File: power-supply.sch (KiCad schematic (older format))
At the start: 108 parts, among them IC1 TPS54561, J12 S2B-PH-K-S_LF__SN_, Q1 BSS138APW, Q2 BSS138APW, Q3 BSS138APW, Q4 BSS138APW, Q5 BSS138APW, U10 TPS62823DLCT, U11 TPS62823DLCT, U12 TPS62823DLCT, U13 TPS62823DLCT, U16 TPS62823DLCT, U9 LM3881MME_NOPB

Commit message: Generated local libs
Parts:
- L2, L3, L4, L5, L6: footprint antmicro-footprints:IHLP-1212AE -> artix-dc-scm-footprints:IHLP-1212AE; symbol antmicroFixedInductors:IHLP1212AEERR47M11 -> artix-dc-scm:IHLP1212AEERR47M11
- Q1, Q2, Q3, Q4, Q5: footprint antmicro-footprints:SC70-3 -> artix-dc-scm-footprints:SC70-3; symbol antmicroTransistorsFETsMOSFETsSingle:BSS138APW -> artix-dc-scm:BSS138APW
- Q6: renamed from Q?; footprint antmicro-footprints:SC70-3 -> artix-dc-scm-footprints:SC70-3; symbol antmicroTransistorsFETsMOSFETsSingle:BSS138APW -> artix-dc-scm:BSS138APW
- R139, R140, R141, R142, R188: footprint antmicro-footprints:0603-res -> artix-dc-scm-footprints:0603-res; symbol antmicroResistors0603:R_0R_0603 -> artix-dc-scm:R_0R_0603
- gave numbers to parts that had none: 3
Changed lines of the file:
@@
 $EndComp
 $Comp
-L antmicroFixedInductors:IHLP1212AEERR47M11 L2
+L artix-dc-scm:IHLP1212AEERR47M11 L2
 U 1 1 605967EC
 P 14275 1350
 F 0 "L2" H 14275 1564 60  0000 C CNN
 F 1 "IHLP1212AEERR47M11" H 14275 1458 60  0000 C CNN
-F 2 "antmicro-footprints:IHLP-1212AE" H 14275 1350 60  0001 C CNN
+F 2 "artix-dc-scm-footprints:IHLP-1212AE" H 14275 1350 60  0001 C CNN
 F 3 "" H 14275 1350 60  0001 C CNN
 F 4 "Vishay" H 14275 1350 50  0001 C CNN "Manufacturer"
@@
 $EndComp
 $Comp
-L antmicroFixedInductors:IHLP1212AEERR47M11 L3
+L artix-dc-scm:IHLP1212AEERR47M11 L3
 U 1 1 605975DC
 P 14300 3275
 F 0 "L3" H 14175 3500 60  0000 C CNN
 F 1 "IHLP1212AEERR47M11" H 14625 3375 60  0000 C CNN
-F 2 "antmicro-footprints:IHLP-1212AE" H 14300 3275 60  0001 C CNN
+F 2 "artix-dc-scm-footprints:IHLP-1212AE" H 14300 3275 60  0001 C CNN
 F 3 "" H 14300 3275 60  0001 C CNN
 F 4 "Vishay" H 14300 3275 50  0001 C CNN "Manufacturer"
@@
 $EndComp
 $Comp
-L antmicroFixedInductors:IHLP1212AEERR47M11 L5
+L artix-dc-scm:IHLP1212AEERR47M11 L5
 U 1 1 605987A7
 P 14350 5100
 F 0 "L5" H 14200 5300 60  0000 C CNN
 F 1 "IHLP1212AEERR47M11" H 14650 5200 60  0000 C CNN
-F 2 "antmicro-footprints:IHLP-1212AE" H 14350 5100 60  0001 C CNN
+F 2 "artix-dc-scm-footprints:IHLP-1212AE" H 14350 5100 60  0001 C CNN
 F 3 "" H 14350 5100 60  0001 C CNN
 F 4 "Vishay" H 14350 5100 50  0001 C CNN "Manufacturer"
@@
 $EndComp
 $Comp
-L antmicroFixedInductors:IHLP1212AEERR47M11 L4
+L artix-dc-scm:IHLP1212AEERR47M11 L4
 U 1 1 605995D0
 P 14325 6825
 F 0 "L4" H 14200 7025 60  0000 C CNN
 F 1 "IHLP1212AEERR47M11" H 14650 6925 60  0000 C CNN
-F 2 "antmicro-footprints:IHLP-1212AE" H 14325 6825 60  0001 C CNN
+F 2 "artix-dc-scm-footprints:IHLP-1212AE" H 14325 6825 60  0001 C CNN
 F 3 "" H 14325 6825 60  0001 C CNN
 F 4 "Vishay" H 14325 6825 50  0001 C CNN "Manufacturer"
@@
 $EndComp
 $Comp
-L antmicroResistors0603:R_0R_0603 R139
+L artix-dc-scm:R_0R_0603 R139
 U 1 1 605E7324
 P 15225 1100
 F 0 "R139" V 15180 1170 60  0000 L CNN
 F 1 "R_0R_0603" H 15225 950 60  0001 C CNN
-F 2 "antmicro-footprints:0603-res" H 15425 1300 60  0001 L CNN
+F 2 "artix-dc-scm-footprints:0603-res" H 15425 1300 60  0001 L CNN
 F 3 "" H 15225 1100 50  0001 C CNN
 F 4 "BOURNS" H 15425 1500 60  0001 L CNN "Manufacturer"
@@
 $EndComp
 $Comp
-L antmicroResistors0603:R_0R_0603 R140
+L artix-dc-scm:R_0R_0603 R140
 U 1 1 605E78C4
 P 15250 3025
 F 0 "R140" V 15205 3095 60  0000 L CNN
 F 1 "R_0R_0603" H 15250 2875 60  0001 C CNN
-F 2 "antmicro-footprints:0603-res" H 15450 3225 60  0001 L CNN
+F 2 "artix-dc-scm-footprints:0603-res" H 15450 3225 60  0001 L CNN
 F 3 "" H 15250 3025 50  0001 C CNN
 F 4 "BOURNS" H 15450 3425 60  0001 L CNN "Manufacturer"
@@
 $EndComp
 $Comp
-L antmicroResistors0603:R_0R_0603 R142
+L artix-dc-scm:R_0R_0603 R142
 U 1 1 605E80F5
 P 15300 4800
 F 0 "R142" V 15255 4870 60  0000 L CNN
 F 1 "R_0R_0603" H 15300 4650 60  0001 C CNN
-F 2 "antmicro-footprints:0603-res" H 15500 5000 60  0001 L CNN
+F 2 "artix-dc-scm-footprints:0603-res" H 15500 5000 60  0001 L CNN
 F 3 "" H 15300 4800 50  0001 C CNN
 F 4 "BOURNS" H 15500 5200 60  0001 L CNN "Manufacturer"
@@
 $EndComp
 $Comp
-L antmicroResistors0603:R_0R_0603 R141
+L artix-dc-scm:R_0R_0603 R141
 U 1 1 605E88AA
 P 15275 6575
 F 0 "R141" V 15230 6645 60  0000 L CNN
 F 1 "R_0R_0603" H 15275 6425 60  0001 C CNN
-F 2 "antmicro-footprints:0603-res" H 15475 6775 60  0001 L CNN
+F 2 "artix-dc-scm-footprints:0603-res" H 15475 6775 60  0001 L CNN
 F 3 "" H 15275 6575 50  0001 C CNN
 F 4 "BOURNS" H 15475 6975 60  0001 L CNN "Manufacturer"
@@
 $EndComp
 $Comp
-L antmicroTransistorsFETsMOSFETsSingle:BSS138APW Q3
+L artix-dc-scm:BSS138APW Q3
 U 1 1 6063EBAE
 P 10275 3975
 F 0 "Q3" H 10383 4028 60  0000 L CNN
 F 1 "BSS138APW" H 10383 3922 60  0000 L CNN
-F 2 "antmicro-footprints:SC70-3" H 10475 4175 60  0001 L CNN
+F 2 "artix-dc-scm-footprints:SC70-3" H 10475 4175 60  0001 L CNN
 F 3 "" H 10475 4275 60  0001 L CNN
 F 4 "BSS138PW" H 10475 4475 60  0001 L CNN "MPN"
@@
 $EndComp
 $Comp
-L antmicroTransistorsFETsMOSFETsSingle:BSS138APW Q4
+L artix-dc-scm:BSS138APW Q4
 U 1 1 60643F19
 P 10300 5200
 F 0 "Q4" H 10408 5253 60  0000 L CNN
 F 1 "BSS138APW" H 10408 5147 60  0000 L CNN
-F 2 "antmicro-footprints:SC70-3" H 10500 5400 60  0001 L CNN
+F 2 "artix-dc-scm-footprints:SC70-3" H 10500 5400 60  0001 L CNN
 F 3 "" H 10500 5500 60  0001 L CNN
 F 4 "BSS138PW" H 10500 5700 60  0001 L CNN "MPN"
@@
 $EndComp
 $Comp
-L antmicroTransistorsFETsMOSFETsSingle:BSS138APW Q1
+L artix-dc-scm:BSS138APW Q1
 U 1 1 60644AF4
 P 10250 6475
 F 0 "Q1" H 10358 6528 60  0000 L CNN
 F 1 "BSS138APW" H 10358 6422 60  0000 L CNN
-F 2 "antmicro-footprints:SC70-3" H 10450 6675 60  0001 L CNN
+F 2 "artix-dc-scm-footprints:SC70-3" H 10450 6675 60  0001 L CNN
 F 3 "" H 10450 6775 60  0001 L CNN
 F 4 "BSS138PW" H 10450 6975 60  0001 L CNN "MPN"
@@
 $EndComp
 $Comp
-L antmicroTransistorsFETsMOSFETsSingle:BSS138APW Q2
+L artix-dc-scm:BSS138APW Q2
 U 1 1 606455AB
 P 10250 7675
 F 0 "Q2" H 10358 7728 60  0000 L CNN
 F 1 "BSS138APW" H 10358 7622 60  0000 L CNN
-F 2 "antmicro-footprints:SC70-3" H 10450 7875 60  0001 L CNN
+F 2 "artix-dc-scm-footprints:SC70-3" H 10450 7875 60  0001 L CNN
 F 3 "" H 10450 7975 60  0001 L CNN
 F 4 "BSS138PW" H 10450 8175 60  0001 L CNN "MPN"
@@
 $EndComp
 $Comp
-L antmicroTransistorsFETsMOSFETsSingle:BSS138APW Q5
+L artix-dc-scm:BSS138APW Q5
 U 1 1 60646CF6
 P 10325 2750
 F 0 "Q5" H 10433 2803 60  0000 L CNN
 F 1 "BSS138APW" H 10433 2697 60  0000 L CNN
-F 2 "antmicro-footprints:SC70-3" H 10525 2950 60  0001 L CNN
+F 2 "artix-dc-scm-footprints:SC70-3" H 10525 2950 60  0001 L CNN
 F 3 "" H 10525 3050 60  0001 L CNN
 F 4 "BSS138PW" H 10525 3250 60  0001 L CNN "MPN"
@@
 	12275 8700 11875 8700
 $Comp
-L antmicroFixedInductors:IHLP1212AEERR47M11 L6
+L artix-dc-scm:IHLP1212AEERR47M11 L6
 U 1 1 6013632B
 P 14325 8550
 F 0 "L6" H 14200 8750 60  0000 C CNN
 F 1 "IHLP1212AEERR47M11" H 14650 8650 60  0000 C CNN
-F 2 "antmicro-footprints:IHLP-1212AE" H 14325 8550 60  0001 C CNN
+F 2 "artix-dc-scm-footprints:IHLP-1212AE" H 14325 8550 60  0001 C CNN
 F 3 "" H 14325 8550 60  0001 C CNN
 F 4 "Vishay" H 14325 8550 50  0001 C CNN "Manufacturer"
@@
 $EndComp
 $Comp
-L antmicroResistors0603:R_0R_0603 R188
+L artix-dc-scm:R_0R_0603 R188
 U 1 1 60136334
 P 15275 8300
 F 0 "R188" V 15230 8370 60  0000 L CNN
 F 1 "R_0R_0603" H 15275 8150 60  0001 C CNN
-F 2 "antmicro-footprints:0603-res" H 15475 8500 60  0001 L CNN
+F 2 "artix-dc-scm-footprints:0603-res" H 15475 8500 60  0001 L CNN
 F 3 "" H 15275 8300 50  0001 C CNN
 F 4 "BOURNS" H 15475 8700 60  0001 L CNN "Manufacturer"
@@
 	10325 1150 10325 1450
 $Comp
-L artix-dc-scm:R_10k_0402 R?
+L artix-dc-scm:R_10k_0402 R189
 U 1 1 60252526
 P 9725 1425
-F 0 "R?" V 9575 1450 60  0000 L CNN
+F 0 "R189" V 9575 1450 60  0000 L CNN
 F 1 "R_10k_0402" H 9725 1275 60  0001 C CNN
 F 2 "artix-dc-scm-footprints:0402-res" H 9925 1625 60  0001 L CNN
@@
 	9725 1575 9725 1750
 $Comp
-L artix-dc-scm:LG_L29K-G2J1-24-Z D?
+L artix-dc-scm:LG_L29K-G2J1-24-Z D14
 U 1 1 60252530
 P 10525 1150
-F 0 "D?" H 10550 1050 60  0000 L CNN
+F 0 "D14" H 10550 1050 60  0000 L CNN
 F 1 "LG_L29K-G2J1-24-Z" H 9650 1375 60  0000 L CNN
 F 2 "artix-dc-scm-footprints:LED_0603" H 10725 1350 60  0001 L CNN
@@
 	10725 1150 10825 1150
 $Comp
-L artix-dc-scm:R_1k_0402 R?
+L artix-dc-scm:R_1k_0402 R190
 U 1 1 6025253B
 P 10975 1150
-F 0 "R?" H 10925 1250 60  0000 C CNN
+F 0 "R190" H 10925 1250 60  0000 C CNN
 F 1 "R_1k_0402" H 10975 1000 60  0001 C CNN
 F 2 "artix-dc-scm-footprints:0402-res" H 11175 1350 60  0001 L CNN
@@
 	11125 1150 11225 1150
 $Comp
-L artix-dc-scm:GND-artix-dc-scm #PWR?
+L artix-dc-scm:GND-artix-dc-scm #PWR06
 U 1 1 60252543
 P 10325 1950
-F 0 "#PWR?" H 10325 1700 50  0001 C CNN
+F 0 "#PWR06" H 10325 1700 50  0001 C CNN
 F 1 "GND" H 10330 1777 50  0000 C CNN
 F 2 "" H 10325 1950 50  0001 C CNN
@@
 VCC5V0
 $Comp
-L antmicroTransistorsFETsMOSFETsSingle:BSS138APW Q?
+L artix-dc-scm:BSS138APW Q6
 U 1 1 60252551
 P 10325 1650
-F 0 "Q?" H 10433 1703 60  0000 L CNN
+F 0 "Q6" H 10433 1703 60  0000 L CNN
 F 1 "BSS138APW" H 10433 1597 60  0000 L CNN
-F 2 "antmicro-footprints:SC70-3" H 10525 1850 60  0001 L CNN
+F 2 "artix-dc-scm-footprints:SC70-3" H 10525 1850 60  0001 L CNN
 F 3 "" H 10525 1950 60  0001 L CNN
 F 4 "BSS138PW" H 10525 2150 60  0001 L CNN "MPN"

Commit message: Cleaned up schematics
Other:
- note removed: "TODO: decide when should this voltage be enabled\n(power sequencer)"
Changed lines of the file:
@@
 Wire Wire Line
 	14575 1350 14875 1350
-Text Notes 14850 1025 0    50   ~ 0
+Text Notes 14850 1075 0    50   ~ 0
 3.3V/3A
 NoConn ~ -625 5725
@@
 U 1 1 60F104BF
 P 5725 4350
-F 0 "D3" H 5808 4403 60  0000 L CNN
-F 1 "PDS760-13" H 5650 4250 60  0000 L CNN
+F 0 "D3" H 5600 4250 60  0000 L CNN
+F 1 "PDS760-13" V 5850 4050 60  0000 L CNN
 F 2 "artix-dc-scm-footprints:PDS760-13" H 5725 4350 60  0001 C CNN
 F 3 "" H 5725 4350 60  0001 C CNN
@@
 Wire Wire Line
 	7150 4425 7150 4600
-Text Notes 3750 2750 0    118  ~ 0
+Text Notes 3750 2750 0    118  ~ 24
 MainSupply (5V 5A)
 $Comp
@@
 Wire Wire Line
 	12975 5400 13300 5400
-Text Notes 15475 3075 0    50   ~ 0
+Text Notes 14875 3000 0    50   ~ 0
 1.8V/3A
-Text Notes 15625 4850 0    50   ~ 0
+Text Notes 14875 4775 0    50   ~ 0
 1.35V/3A
 Connection ~ 14200 5900
@@
 	1    0    0    -1
 $EndComp
-Text Notes 9450 825  0    118  ~ 0
+Text Notes 9450 825  0    118  ~ 24
 PWR_LED Indicators
 Wire Notes Line
@@
 Text Label 5600 9100 2    50   ~ 0
 VCCIO_EN
-Text Notes 13125 950  0    118  ~ 0
+Text Notes 13125 950  0    118  ~ 24
 3V3 supply
-Text Notes 13200 2825 0    118  ~ 0
+Text Notes 13200 2825 0    118  ~ 24
 1V8 supply
-Text Notes 13150 4750 0    118  ~ 0
+Text Notes 13150 4750 0    118  ~ 24
 1V35 supply
 Wire Wire Line
@@
 Wire Wire Line
 	12950 7125 13275 7125
-Text Notes 15675 6575 0    50   ~ 0
+Text Notes 14900 6550 0    50   ~ 0
 1.0V/3A
 Connection ~ 14175 7625
@@
 	1    0    0    -1
 $EndComp
-Text Notes 13125 6475 0    118  ~ 0
+Text Notes 13125 6475 0    118  ~ 24
 1V0 supply
 Wire Wire Line
@@
 U 1 1 6113B8AB
 P 4500 9000
-F 0 "U9" H 4250 9325 50  0000 C CNN
-F 1 "LM3881MME_NOPB" H 4575 9275 50  0000 C CNN
+F 0 "U9" H 4475 9350 50  0000 C CNN
+F 1 "LM3881MME_NOPB" H 4475 9250 50  0000 C CNN
 F 2 "artix-dc-scm-footprints:VSSOP8-Texas_Instruments-DGK0008A" H 4500 9400 50  0001 L CNN
 F 3 "http://www.ti.com/lit/ds/symlink/lm3881.pdf" H 4500 9500 50  0001 L CNN
@@
 U 1 1 5FFECF1E
 P 4975 8575
-F 0 "R63" V 4930 8645 60  0000 L CNN
+F 0 "R63" H 5100 8550 60  0000 L CNN
 F 1 "R_1k_0402" H 4975 8425 60  0001 C CNN
 F 2 "artix-dc-scm-footprints:0402-res" H 5175 8775 60  0001 L CNN
@@
 F 4 "BOURNS" H 5175 8975 60  0001 L CNN "Manufacturer"
 F 5 "CR0402-FX-1001GLF" H 5175 8875 60  0001 L CNN "MPN"
-F 6 "1k" V 5028 8645 50  0000 L CNN "Val"
+F 6 "1k" H 4950 8575 50  0000 L CNN "Val"
 	1    4975 8575
 	0    1    1    0
@@
 U 1 1 5FFED382
 P 5075 8575
-F 0 "R64" V 5030 8645 60  0000 L CNN
+F 0 "R64" H 5200 8550 60  0000 L CNN
 F 1 "R_1k_0402" H 5075 8425 60  0001 C CNN
 F 2 "artix-dc-scm-footprints:0402-res" H 5275 8775 60  0001 L CNN
@@
 F 4 "BOURNS" H 5275 8975 60  0001 L CNN "Manufacturer"
 F 5 "CR0402-FX-1001GLF" H 5275 8875 60  0001 L CNN "MPN"
-F 6 "1k" V 5128 8645 50  0000 L CNN "Val"
+F 6 "1k" H 5050 8575 50  0000 L CNN "Val"
 	1    5075 8575
 	0    1    1    0
@@
 U 1 1 5FFED63B
 P 5175 8575
-F 0 "R65" V 5130 8645 60  0000 L CNN
+F 0 "R65" H 5300 8550 60  0000 L CNN
 F 1 "R_1k_0402" H 5175 8425 60  0001 C CNN
 F 2 "artix-dc-scm-footprints:0402-res" H 5375 8775 60  0001 L CNN
@@
 F 4 "BOURNS" H 5375 8975 60  0001 L CNN "Manufacturer"
 F 5 "CR0402-FX-1001GLF" H 5375 8875 60  0001 L CNN "MPN"
-F 6 "1k" V 5228 8645 50  0000 L CNN "Val"
+F 6 "1k" H 5150 8575 50  0000 L CNN "Val"
 	1    5175 8575
 	0    1    1    0
@@
 U 1 1 60986D60
 P 10525 2250
-F 0 "D8" H 10550 2150 60  0000 L CNN
+F 0 "D8" H 10450 2100 60  0000 L CNN
 F 1 "LG_L29K-G2J1-24-Z" H 9650 2475 60  0000 L CNN
 F 2 "artix-dc-scm-footprints:LED_0603" H 10725 2450 60  0001 L CNN
@@
 U 1 1 60986D95
 P 10475 3475
-F 0 "D6" H 10500 3375 60  0000 L CNN
+F 0 "D6" H 10400 3325 60  0000 L CNN
 F 1 "LG_L29K-G2J1-24-Z" H 9600 3700 60  0000 L CNN
 F 2 "artix-dc-scm-footprints:LED_0603" H 10675 3675 60  0001 L CNN
@@
 U 1 1 60986DCA
 P 10500 4700
-F 0 "D7" H 10525 4600 60  0000 L CNN
+F 0 "D7" H 10425 4525 60  0000 L CNN
 F 1 "LG_L29K-G2J1-24-Z" H 9625 4925 60  0000 L CNN
 F 2 "artix-dc-scm-footprints:LED_0603" H 10700 4900 60  0001 L CNN
@@
 U 1 1 60986DFE
 P 10450 5975
-F 0 "D4" H 10475 5875 60  0000 L CNN
+F 0 "D4" H 10375 5825 60  0000 L CNN
 F 1 "LG_L29K-G2J1-24-Z" H 9575 6200 60  0000 L CNN
 F 2 "artix-dc-scm-footprints:LED_0603" H 10650 6175 60  0001 L CNN
@@
 U 1 1 60986E30
 P 10450 7175
-F 0 "D5" H 10475 7075 60  0000 L CNN
+F 0 "D5" H 10375 7025 60  0000 L CNN
 F 1 "LG_L29K-G2J1-24-Z" H 9575 7400 60  0000 L CNN
 F 2 "artix-dc-scm-footprints:LED_0603" H 10650 7375 60  0001 L CNN
@@
 Text GLabel 1625 2250 0    50   Input ~ 0
 P12V_AUX
-Text Notes 1300 925  0    118  ~ 0
+Text Notes 1300 925  0    118  ~ 24
 External 12V supply
 $Comp
@@
 U 1 1 6003348A
 P 3725 8625
-F 0 "R62" V 3680 8695 60  0000 L CNN
+F 0 "R62" H 3650 8725 60  0000 L CNN
 F 1 "R_1k_0402" H 3725 8475 60  0001 C CNN
 F 2 "artix-dc-scm-footprints:0402-res" H 3925 8825 60  0001 L CNN
@@
 F 4 "BOURNS" H 3925 9025 60  0001 L CNN "Manufacturer"
 F 5 "CR0402-FX-1001GLF" H 3925 8925 60  0001 L CNN "MPN"
-F 6 "1k" V 3778 8695 50  0000 L CNN "Val"
+F 6 "1k" H 3675 8625 50  0000 L CNN "Val"
 	1    3725 8625
 	0    1    1    0
@@
 U 1 1 619949C4
 P 3200 1675
-F 0 "C14" H 3315 1720 60  0000 L CNN
+F 0 "C14" V 3125 1725 60  0000 L CNN
 F 1 "C_10u_25V_0603" H 3200 1525 60  0001 C CNN
 F 2 "artix-dc-scm-footprints:0603-cap" H 3400 1875 60  0001 L CNN
@@
 F 4 "TDK" H 3400 2075 60  0001 L CNN "Manufacturer"
 F 5 "C1608X5R1E106M080AC" H 3400 1975 60  0001 L CNN "MPN"
-F 6 "10u/25V" H 3315 1622 50  0000 L CNN "Val"
+F 6 "10u/25V" V 3325 1500 50  0000 L CNN "Val"
 	1    3200 1675
 	1    0    0    -1
@@
 U 1 1 619975A1
 P 3475 1675
-F 0 "C15" H 3590 1720 60  0000 L CNN
+F 0 "C15" V 3400 1725 60  0000 L CNN
 F 1 "C_10u_25V_0603" H 3475 1525 60  0001 C CNN
 F 2 "artix-dc-scm-footprints:0603-cap" H 3675 1875 60  0001 L CNN
@@
 F 4 "TDK" H 3675 2075 60  0001 L CNN "Manufacturer"
 F 5 "C1608X5R1E106M080AC" H 3675 1975 60  0001 L CNN "MPN"
-F 6 "10u/25V" H 3590 1622 50  0000 L CNN "Val"
+F 6 "10u/25V" V 3600 1500 50  0000 L CNN "Val"
 	1    3475 1675
 	1    0    0    -1
@@
 U 1 1 619977B0
 P 3750 1675
-F 0 "C16" H 3865 1720 60  0000 L CNN
+F 0 "C16" V 3700 1725 60  0000 L CNN
 F 1 "C_10u_25V_0603" H 3750 1525 60  0001 C CNN
 F 2 "artix-dc-scm-footprints:0603-cap" H 3950 1875 60  0001 L CNN
@@
 F 4 "TDK" H 3950 2075 60  0001 L CNN "Manufacturer"
 F 5 "C1608X5R1E106M080AC" H 3950 1975 60  0001 L CNN "MPN"
-F 6 "10u/25V" H 3865 1622 50  0000 L CNN "Val"
+F 6 "10u/25V" V 3875 1500 50  0000 L CNN "Val"
 	1    3750 1675
 	1    0    0    -1
@@
 U 1 1 619982FA
 P 4025 1675
-F 0 "C17" H 4140 1720 60  0000 L CNN
+F 0 "C17" H 4075 1775 60  0000 L CNN
 F 1 "C_100n_0402_16V" H 4025 1525 60  0001 C CNN
 F 2 "artix-dc-scm-footprints:0402-cap" H 4225 1875 60  0001 L CNN
@@
 Wire Wire Line
 	12950 8850 13275 8850
-Text Notes 15525 8025 0    50   ~ 0
+Text Notes 14900 8275 0    50   ~ 0
 1.2V/3A
 Connection ~ 14175 9350
@@
 	1    0    0    -1
 $EndComp
-Text Notes 13125 8200 0    118  ~ 0
+Text Notes 13125 8200 0    118  ~ 24
 1V2 supply
 Wire Wire Line
@@
 	-1   0    0    1
 $EndComp
-Text Label 12275 8700 2    50   ~ 0
-VCCINT_EN
 Wire Wire Line
 	12575 8700 13275 8700
@@
 	0    1    1    0
 $EndComp
-Text Notes 10625 8675 0    50   ~ 0
-TODO: decide when should this voltage be enabled\n(power sequencer)
 $Comp
 L artix-dc-scm:R_100k_0402 R186
@@
 U 1 1 60252530
 P 10525 1150
-F 0 "D14" H 10550 1050 60  0000 L CNN
+F 0 "D14" H 10425 1000 60  0000 L CNN
 F 1 "LG_L29K-G2J1-24-Z" H 9650 1375 60  0000 L CNN
 F 2 "artix-dc-scm-footprints:LED_0603" H 10725 1350 60  0001 L CNN
@@
 	1    0    0    -1
 $EndComp
+Text Label 12225 8700 2    50   ~ 0
+VCCIO_EN
 $EndSCHEMATC

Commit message: Make DRC clean
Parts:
- removed C17: C_100n_0402_16V, artix-dc-scm-footprints:0402-cap, symbol artix-dc-scm:C_100n_0402_16V
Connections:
- wire segments 354 -> 350
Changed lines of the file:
@@
-	1    0    0    -1
-$EndComp
-$Comp
-L artix-dc-scm:C_100n_0402_16V C17
-U 1 1 619982FA
-P 4025 1675
-F 0 "C17" H 4075 1775 60  0000 L CNN
-F 1 "C_100n_0402_16V" H 4025 1525 60  0001 C CNN
-F 2 "artix-dc-scm-footprints:0402-cap" H 4225 1875 60  0001 L CNN
-F 3 "" H 4025 1675 50  0001 C CNN
-F 4 "MULTICOMP" H 4225 2075 60  0001 L CNN "Manufacturer"
-F 5 "MC0402B104K160CT" H 4225 1975 60  0001 L CNN "MPN"
-F 6 "100n" H 4140 1622 50  0000 L CNN "Val"
-	1    4025 1675
 	1    0    0    -1
 $EndComp
@@
 Wire Wire Line
 	3200 1450 3475 1450
-Wire Wire Line
-	4025 1450 4025 1525
 Connection ~ 3200 1450
 Wire Wire Line
@@
 Wire Wire Line
 	3750 1525 3750 1450
-Connection ~ 3750 1450
-Wire Wire Line
-	3750 1450 4025 1450
 Wire Wire Line
 	3475 1525 3475 1450
@@
 Wire Wire Line
 	3200 1900 3200 2000
-Wire Wire Line
-	4025 1825 4025 1900
-Wire Wire Line
-	4025 1900 3750 1900
 Connection ~ 3475 1900
 Wire Wire Line
 	3750 1825 3750 1900
-Connection ~ 3750 1900
 Wire Wire Line
 	3750 1900 3475 1900

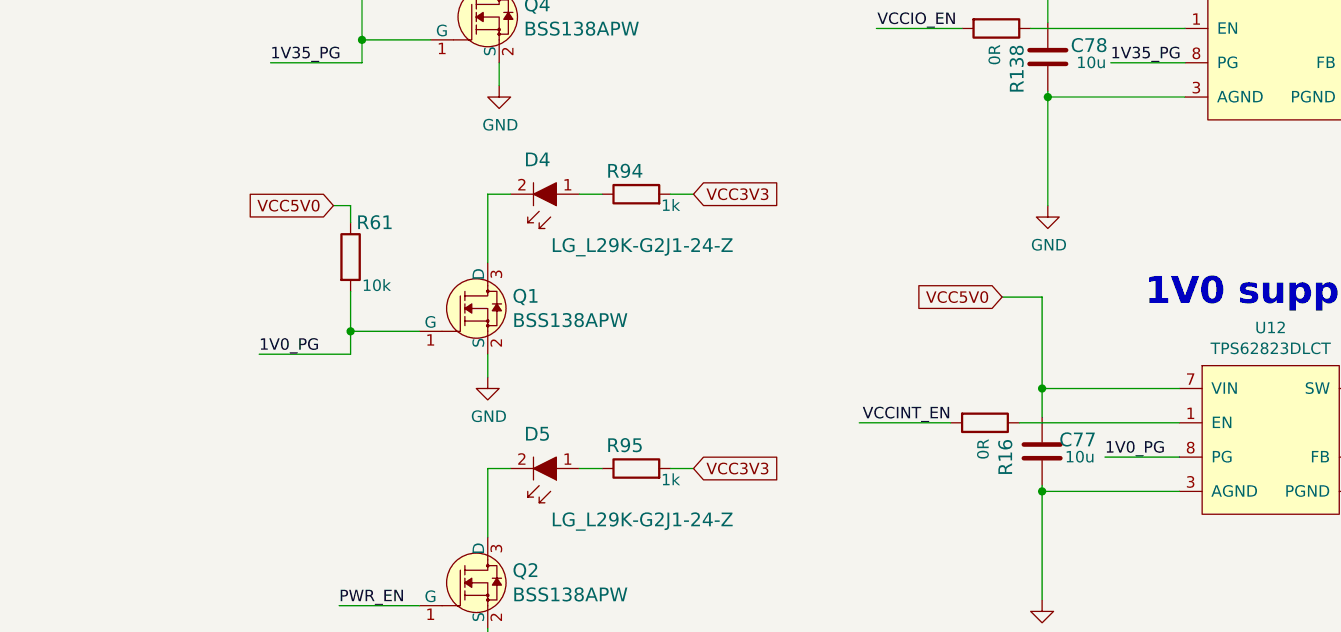
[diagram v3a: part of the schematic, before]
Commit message: Fix 1v0 translator
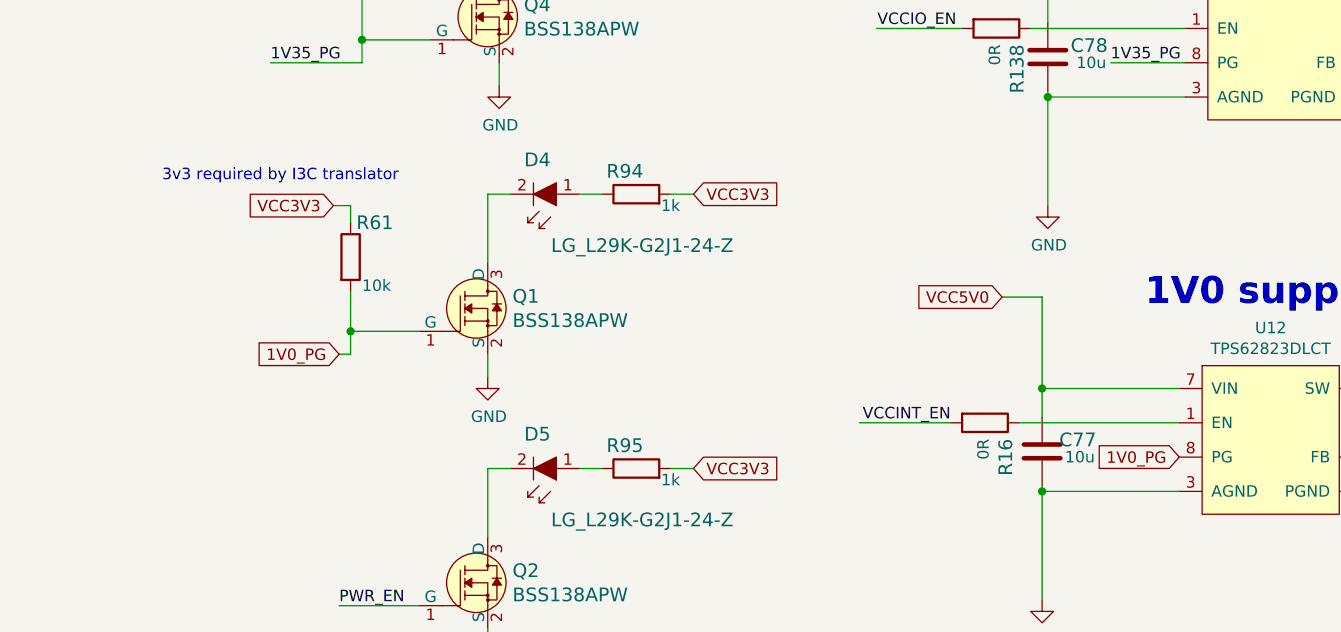
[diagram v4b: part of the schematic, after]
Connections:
- net VCC3V3: now also R61.1
- net VCC5V0: no longer R61.1
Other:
- note added: "3v3 required by I3C translator"
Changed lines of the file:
@@
 Wire Wire Line
 	14175 7275 14075 7275
-Text Label 12950 7125 0    50   ~ 0
-1V0_PG
 Wire Wire Line
 	14175 7625 14925 7625
@@
 Wire Wire Line
 	15275 6725 15275 6825
-Wire Wire Line
-	12950 7125 13275 7125
 Text Notes 14900 6550 0    50   ~ 0
 1.0V/3A
@@
 Wire Wire Line
 	9650 6575 9650 6675
-Wire Wire Line
-	9650 6675 9250 6675
 Connection ~ 9650 6575
-Text Label 9250 6675 0    50   ~ 0
-1V0_PG
 $Comp
 L artix-dc-scm:R_0R_1206 R69
@@
 VCC5V0
 Text GLabel 9625 3525 0    50   Input ~ 0
-VCC5V0
-Text GLabel 9625 4750 0    50   Input ~ 0
-VCC5V0
-Text GLabel 9575 6025 0    50   Input ~ 0
 VCC5V0
 Wire Wire Line
@@
 Text Label 12225 8700 2    50   ~ 0
 VCCIO_EN
+Text GLabel 9625 4750 0    50   Input ~ 0
+VCC5V0
+Text GLabel 9575 6025 0    50   Input ~ 0
+VCC3V3
+Text GLabel 13275 7125 0    50   Input ~ 0
+1V0_PG
+Wire Wire Line
+	9650 6675 9600 6675
+Text GLabel 9600 6675 0    50   Input ~ 0
+1V0_PG
+Text Notes 8825 5925 0    50   ~ 0
+3v3 required by I3C translator
 $EndSCHEMATC
